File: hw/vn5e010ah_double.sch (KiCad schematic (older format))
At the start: 6 parts, among them U1201 VN5E010AH, U1202 VN5E010AH

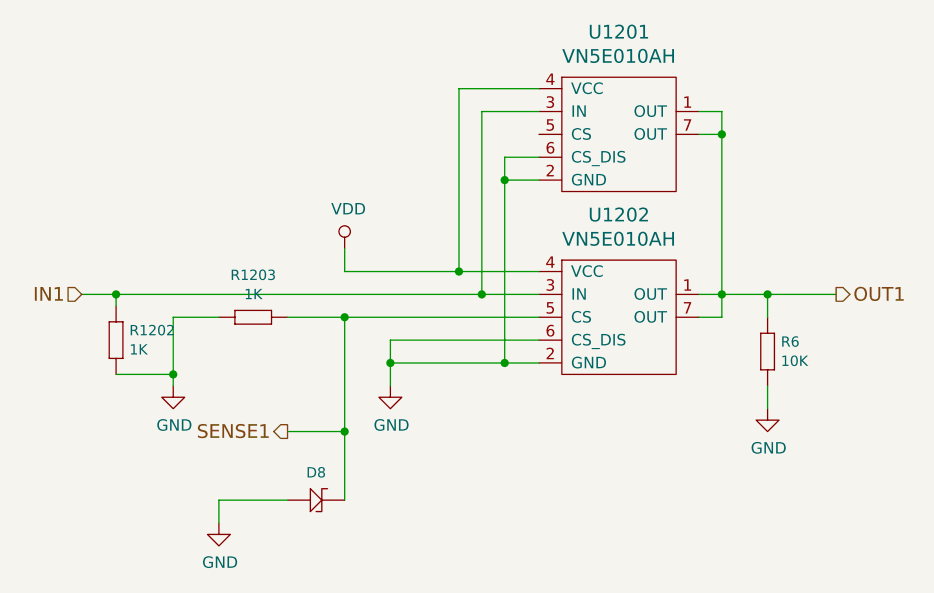
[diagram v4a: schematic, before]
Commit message: radiator fet added to pcb, but not yet ready
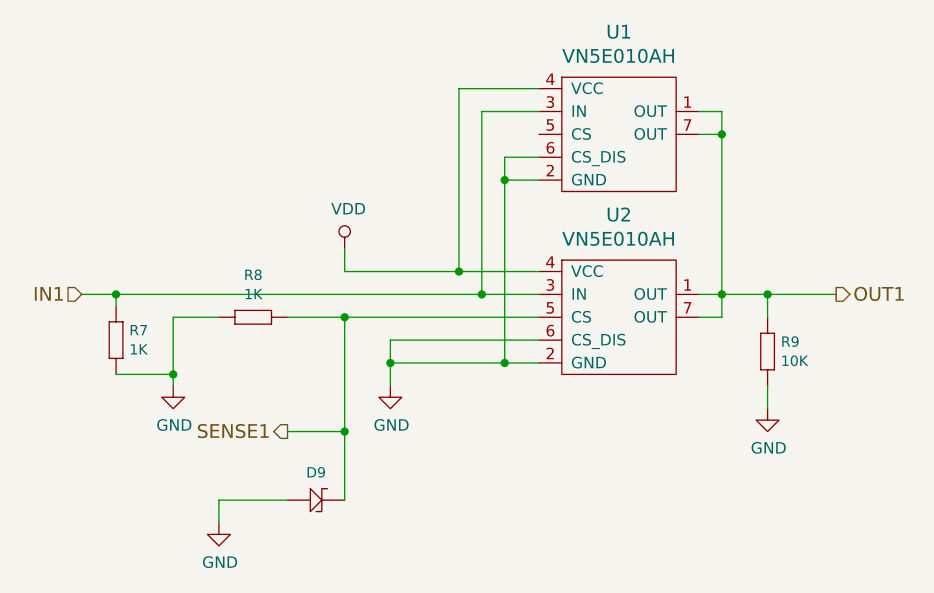
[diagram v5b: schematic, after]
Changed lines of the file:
@@
 $Descr A4 11693 8268
 encoding utf-8
-Sheet 12 12
+Sheet 13 13
 Title ""
 Date ""
@@
 AR Path="/5B1A3D6E/5B1A4079" Ref="#PWR01203"  Part="1"
 AR Path="/5A13680F/5B1A4079" Ref="#PWR01103"  Part="1"
-F 0 "#PWR01203" H 5450 3150 50  0001 C CNN
+AR Path="/5C202EB2/5B1A4079" Ref="#PWR0104"  Part="1"
+F 0 "#PWR0104" H 5450 3150 50  0001 C CNN
 F 1 "VDD" H 5467 3473 50  0000 C CNN
 F 2 "" H 5450 3300 50  0000 C CNN
@@
 AR Path="/5B1A3D6E/5B1A4087" Ref="#PWR01201"  Part="1"
 AR Path="/5A13680F/5B1A4087" Ref="#PWR01101"  Part="1"
-F 0 "#PWR01201" H 4700 3650 50  0001 C CNN
+AR Path="/5C202EB2/5B1A4087" Ref="#PWR0105"  Part="1"
+F 0 "#PWR0105" H 4700 3650 50  0001 C CNN
 F 1 "GND" H 4705 3727 50  0000 C CNN
 F 2 "" H 4700 3900 50  0000 C CNN
@@
 AR Path="/5A14370A/5B1A4092" Ref="R?"  Part="1"
 AR Path="/5B1A3D6E/5B1A4092" Ref="R1202"  Part="1"
-F 0 "R1202" V 4458 3708 45  0000 L CNN
+AR Path="/5C202EB2/5B1A4092" Ref="R7"  Part="1"
+F 0 "R7" V 4458 3708 45  0000 L CNN
 F 1 "1K" V 4542 3708 45  0000 L CNN
 F 2 "yageo:0603" H 4480 3800 20  0001 C CNN
@@
 AR Path="/5B1A3D6E/5B1A40AC" Ref="U1202"  Part="1"
 AR Path="/5A13680F/5B1A40AC" Ref="U1103"  Part="1"
-F 0 "U1202" H 6650 4047 60  0000 C CNN
+AR Path="/5C202EB2/5B1A40AC" Ref="U2"  Part="1"
+F 0 "U2" H 6650 4047 60  0000 C CNN
 F 1 "VN5E010AH" H 6650 3941 60  0000 C CNN
 F 2 "usevolt:HPAK" H 6350 4550 60  0001 C CNN
@@
 AR Path="/5B1A3D6E/5B1A40B3" Ref="#PWR01204"  Part="1"
 AR Path="/5A13680F/5B1A40B3" Ref="#PWR01104"  Part="1"
-F 0 "#PWR01204" H 5650 3650 50  0001 C CNN
+AR Path="/5C202EB2/5B1A40B3" Ref="#PWR0112"  Part="1"
+F 0 "#PWR0112" H 5650 3650 50  0001 C CNN
 F 1 "GND" H 5655 3727 50  0000 C CNN
 F 2 "" H 5650 3900 50  0000 C CNN
@@
 AR Path="/5B1A3D6E/5B1A4293" Ref="U1201"  Part="1"
 AR Path="/5A13680F/5B1A4293" Ref="U1102"  Part="1"
-F 0 "U1201" H 6650 3247 60  0000 C CNN
+AR Path="/5C202EB2/5B1A4293" Ref="U1"  Part="1"
+F 0 "U1" H 6650 3247 60  0000 C CNN
 F 1 "VN5E010AH" H 6650 3141 60  0000 C CNN
 F 2 "usevolt:HPAK" H 6350 3750 60  0001 C CNN
@@
 AR Path="/5B1A3D6E/5B2322BF" Ref="R1203"  Part="1"
 AR Path="/5A13680F/5B2322BF" Ref="R1102"  Part="1"
-F 0 "R1203" H 5050 3784 45  0000 C CNN
+AR Path="/5C202EB2/5B2322BF" Ref="R8"  Part="1"
+F 0 "R8" H 5050 3784 45  0000 C CNN
 F 1 "1K" H 5050 3700 45  0000 C CNN
 F 2 "yageo:0603" H 5030 3750 20  0001 C CNN
@@
 AR Path="/5B1A3D6E/5BA96DF9" Ref="R6"  Part="1"
 AR Path="/5A13680F/5BA96DF9" Ref="R5"  Part="1"
-F 0 "R6" V 7308 3758 45  0000 L CNN
+AR Path="/5C202EB2/5BA96DF9" Ref="R9"  Part="1"
+F 0 "R9" V 7308 3758 45  0000 L CNN
 F 1 "10K" V 7392 3758 45  0000 L CNN
 F 2 "yageo:0603" H 7330 3850 20  0001 C CNN
@@
 AR Path="/5B1A3D6E/5BA9746E" Ref="#PWR0111"  Part="1"
 AR Path="/5A13680F/5BA9746E" Ref="#PWR0110"  Part="1"
-F 0 "#PWR0111" H 7300 3750 50  0001 C CNN
+AR Path="/5C202EB2/5BA9746E" Ref="#PWR0113"  Part="1"
+F 0 "#PWR0113" H 7300 3750 50  0001 C CNN
 F 1 "GND" H 7305 3827 50  0000 C CNN
 F 2 "" H 7300 4000 50  0000 C CNN
@@
 AR Path="/5B1A3D6E/5BAAE03B" Ref="D8"  Part="1"
 AR Path="/5A13680F/5BAAE03B" Ref="D7"  Part="1"
-F 0 "D8" H 5325 4520 45  0000 C CNN
+AR Path="/5C202EB2/5BAAE03B" Ref="D9"  Part="1"
+F 0 "D9" H 5325 4520 45  0000 C CNN
 F 1 "ZENER_MM3Z3V6T1G" H 5675 4775 45  0001 L BNN
 F 2 "usevolt:SOD-323" H 5375 4775 20  0001 C CNN
@@
 AR Path="/5B1A3D6E/5BAAE0D6" Ref="#PWR0103"  Part="1"
 AR Path="/5A13680F/5BAAE0D6" Ref="#PWR0102"  Part="1"
-F 0 "#PWR0103" H 4900 4250 50  0001 C CNN
+AR Path="/5C202EB2/5BAAE0D6" Ref="#PWR0114"  Part="1"
+F 0 "#PWR0114" H 4900 4250 50  0001 C CNN
 F 1 "GND" H 4905 4327 50  0000 C CNN
 F 2 "" H 4900 4500 50  0000 C CNN
